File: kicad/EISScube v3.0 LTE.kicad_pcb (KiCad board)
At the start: 4 copper layers, 100 x 72 mm, 255 parts, among them J1 Boot, J2 UART, J3 JTag, J4 SIM_Card_w_det_sw, J5 USB_B_Mini, J6 Screw_Terminal_01x08, K1 SANYOU_SRD_Form_C, Q2 GSM3612PJZF, Q3 GSM3612PJZF, Q4 GSM3612PJZF, Q5 GSM3612PJZF, SW1 Reset, U1 STM32L051C8Tx, U2 SN74LV1T34DBVR, U3 U-Blox-SARA-R4, U4 LM2576HVS-12, U5 MIC29302WU-TR, U6 L7805, U7 LM1117-3.3, U8 LM1117-1.8, U9 LTV-357T, Y1 12MHz, Y2 32.768KHz

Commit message: Changes for enclosure case
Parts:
- removed the REF** at (160.0, 122.2)
- removed the REF** at (180.3, 122.6)
- removed the REF** at (180.3, 115.4)
- removed the REF** at (180.3, 110.4)
- removed the REF** at (180.3, 105.4)
- removed the REF** at (185.4, 122.6)
- removed the REF** at (175.3, 122.6)
- removed the REF** at (128.8, 94.3)
- removed the REF** at (138.8, 94.3)
- removed the REF** at (143.8, 89.3)
- removed the REF** at (120.4, 123.1)
- removed the REF** at (121.4, 124.2)
- removed the REF** at (114.6, 126.0)
- removed the REF** at (115.1, 121.0)
- added REF**: VIA-0.6mm, EISScube_LTE:VIA-0.6mm, F.Cu at (134.4, 126.0)
- added REF**: VIA-0.6mm, EISScube_LTE:VIA-0.6mm, F.Cu at (104.9, 116.3)
- added REF**: VIA-0.6mm, EISScube_LTE:VIA-0.6mm, F.Cu at (170.1, 111.3)
- added REF**: VIA-0.6mm, EISScube_LTE:VIA-0.6mm, F.Cu at (168.5, 112.8)
- added REF**: VIA-0.6mm, EISScube_LTE:VIA-0.6mm, F.Cu at (166.9, 114.4)
- added REF**: VIA-0.6mm, EISScube_LTE:VIA-0.6mm, F.Cu at (165.2, 116.1)
- added REF**: VIA-0.6mm, EISScube_LTE:VIA-0.6mm, F.Cu at (173.0, 124.5)
- added REF**: VIA-0.6mm, EISScube_LTE:VIA-0.6mm, F.Cu at (173.0, 123.2)
- added REF**: VIA-0.6mm, EISScube_LTE:VIA-0.6mm, F.Cu at (162.8, 121.9)
- added REF**: VIA-0.6mm, EISScube_LTE:VIA-0.6mm, F.Cu at (162.8, 124.5)
- added REF**: VIA-0.6mm, EISScube_LTE:VIA-0.6mm, F.Cu at (169.2, 118.4)
- added REF**: VIA-0.6mm, EISScube_LTE:VIA-0.6mm, F.Cu at (167.9, 124.5)
- added REF**: VIA-0.6mm, EISScube_LTE:VIA-0.6mm, F.Cu at (175.3, 115.7)
- added REF**: VIA-0.6mm, EISScube_LTE:VIA-0.6mm, F.Cu at (135.4, 123.7)
- added REF**: VIA-0.6mm, EISScube_LTE:VIA-0.6mm, F.Cu at (177.8, 115.7)
- added REF**: VIA-0.6mm, EISScube_LTE:VIA-0.6mm, F.Cu at (167.9, 121.9)
- added REF**: VIA-0.6mm, EISScube_LTE:VIA-0.6mm, F.Cu at (167.9, 119.8)
- added REF**: VIA-0.6mm, EISScube_LTE:VIA-0.6mm, F.Cu at (170.7, 116.8)
- added REF**: VIA-0.6mm, EISScube_LTE:VIA-0.6mm, F.Cu at (172.7, 115.7)
- added REF**: VIA-0.6mm, EISScube_LTE:VIA-0.6mm, F.Cu at (180.3, 115.7)
- added REF**: VIA-0.6mm, EISScube_LTE:VIA-0.6mm, F.Cu at (182.9, 115.7)
- added REF**: VIA-0.6mm, EISScube_LTE:VIA-0.6mm, F.Cu at (133.3, 123.7)
- added REF**: VIA-0.6mm, EISScube_LTE:VIA-0.6mm, F.Cu at (148.0, 118.7)
- added REF**: VIA-0.6mm, EISScube_LTE:VIA-0.6mm, F.Cu at (149.2, 114.9)
- added REF**: VIA-0.6mm, EISScube_LTE:VIA-0.6mm, F.Cu at (155.6, 112.4)
- added REF**: VIA-0.6mm, EISScube_LTE:VIA-0.6mm, F.Cu at (155.6, 114.9)
- added REF**: VIA-0.6mm, EISScube_LTE:VIA-0.6mm, F.Cu at (155.6, 121.3)
- added REF**: VIA-0.6mm, EISScube_LTE:VIA-0.6mm, F.Cu at (153.0, 121.3)
- AE1: value Antenna_Shield -> Antenna
- C35, C36, C37, C8, R24: moved to F.Cu
- J4: value SIM_Card_w_det_sw -> SIM card holder
- J6: value Screw_Terminal_01x08 -> Connector 1 x 8
- K1: value SANYOU_SRD_Form_C -> SRD Form C
- R23: moved to B.Cu
- REF**: footprint Mounting_Holes:MountingHole_3.2mm_M3_Pad_Via -> Mounting_Holes:MountingHole_2.7mm_Pad
- REF** (x3): footprint Mounting_Holes:MountingHole_3.2mm_M3_Pad_Via -> Mounting_Holes:MountingHole_2.7mm_M2.5_Pad
- moved REF** 67.9 mm to (103.5, 132.1)
- moved REF** 63.4 mm to (99.7, 132.1)
- moved REF** 50.1 mm to (99.7, 117.5)
- moved REF** 49.2 mm to (99.7, 81.3)
- moved REF** 48.3 mm to (99.7, 113.7)
- moved REF** 48.0 mm to (103.5, 109.9)
- moved REF** 44.0 mm to (99.7, 106.0)
- moved D10 38.6 mm to (137.7, 82.5), turned to 270 degrees
- moved REF** 36.3 mm to (112.4, 87.6)
- moved D8 35.8 mm to (135.1, 82.5), turned to 270 degrees
- moved D11 34.3 mm to (141.1, 98.3), turned to 90 degrees
- moved REF** 33.9 mm to (108.6, 87.0)
- moved C41 33.2 mm to (149.1, 121.2), turned to 180 degrees
- moved REF** 33.1 mm to (122.6, 110.5)
- moved C21 33.0 mm to (132.6, 82.4), turned to 90 degrees
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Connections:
- D14 pad 3: 24VAC-2 -> 24VAC-1
- D14 pad 4: 24VAC-1 -> 24VAC-2
- J4 pad C6: Net-(J4-PadC6) -> (no net)
- J5 pad 4: Net-(J5-Pad4) -> (no net)
- U1 pad 16: Net-(U1-Pad16) -> (no net)
- U1 pad 17: Net-(U1-Pad17) -> (no net)
- U1 pad 19: Net-(U1-Pad19) -> (no net)
- U1 pad 2: Net-(U1-Pad2) -> (no net)
- U1 pad 20: Net-(U1-Pad20) -> (no net)
- U1 pad 25: Net-(U1-Pad25) -> (no net)
- U1 pad 26: Net-(U1-Pad26) -> (no net)
- U1 pad 27: Net-(U1-Pad27) -> (no net)
- U1 pad 28: Net-(U1-Pad28) -> (no net)
- U1 pad 29: Net-(U1-Pad29) -> (no net)
- U1 pad 38: Net-(U1-Pad38) -> (no net)
- U1 pad 41: Net-(U1-Pad41) -> (no net)
- U1 pad 42: Net-(U1-Pad42) -> (no net)
- U1 pad 43: Net-(U1-Pad43) -> (no net)
- U1 pad 46: Net-(U1-Pad46) -> (no net)
- U2 pad 1: Net-(U2-Pad1) -> (no net)
- U3 pad 19: Net-(U3-Pad19) -> (no net)
- U3 pad 2: Net-(U3-Pad2) -> (no net)
- U3 pad 23: Net-(U3-Pad23) -> (no net)
- U3 pad 24: Net-(U3-Pad24) -> (no net)
- U3 pad 25: Net-(U3-Pad25) -> (no net)
- U3 pad 26: Net-(U3-Pad26) -> (no net)
- U3 pad 27: Net-(U3-Pad27) -> (no net)
- U3 pad 31: Net-(U3-Pad31) -> (no net)
- U3 pad 33: Net-(U3-Pad33) -> (no net)
- U3 pad 34: Net-(U3-Pad34) -> (no net)
- U3 pad 35: Net-(U3-Pad35) -> (no net)
- U3 pad 36: Net-(U3-Pad36) -> (no net)
- U3 pad 37: Net-(U3-Pad37) -> (no net)
- U3 pad 44: Net-(U3-Pad44) -> (no net)
- U3 pad 45: Net-(U3-Pad45) -> (no net)
- U3 pad 46: Net-(U3-Pad46) -> (no net)
- U3 pad 47: Net-(U3-Pad47) -> (no net)
- U3 pad 48: Net-(U3-Pad48) -> (no net)
- U3 pad 49: Net-(U3-Pad49) -> (no net)
- U3 pad 6: Net-(U3-Pad6) -> (no net)
- U3 pad 7: Net-(U3-Pad7) -> (no net)
- U3 pad 8: Net-(U3-Pad8) -> (no net)
- U3 pad 9: Net-(U3-Pad9) -> (no net)
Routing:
- net /EISScube-pw/COM: track 0.00 -> 133.3 mm
- net /EISScube-pw/NC: track 0.07 -> 108.1 mm
- net +12V: track 93.1 -> 131.3 mm, vias 2 -> 1
- net /EISScube-pw/NO: track 0.00 -> 27.4 mm
- net GND: track 55.8 -> 30.8 mm, vias 1 -> 0
- net /EISScube-cl/V_INT: track 50.3 -> 27.0 mm
- net +1V8: track 100.9 -> 120.4 mm
- net /EISScube-pw/+5V: track 39.4 -> 58.5 mm, vias 0 -> 1
- net +3V3: track 48.0 -> 64.5 mm, vias 1 -> 2
- net /EISScube-cl/VSIM: track 33.6 -> 48.4 mm
- net INPUT: track 56.9 -> 43.1 mm, vias 0 -> 1
- net /EISScube-cl/SIM_RST: track 33.7 -> 47.3 mm
- net NRST: track 43.1 -> 30.0 mm, vias 2 -> 1
- net Net-(D15-Pad1): track 18.5 -> 30.8 mm
- net /EISScube-cl/SIM_CLK: track 35.0 -> 46.4 mm
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- removed copper zone on B.Cu, net +12V
- removed copper zone on F.Cu, net +12V
- removed copper zone on In1.Cu, net +12V
- removed copper zone on In2.Cu, net +12V
- removed copper zone on B.Cu, net /EISScube-pw/COM
- removed copper zone on F.Cu, net /EISScube-pw/COM
- removed copper zone on In1.Cu, net /EISScube-pw/COM
- removed copper zone on In2.Cu, net /EISScube-pw/COM
- removed copper zone on B.Cu, net /EISScube-pw/NC
- removed copper zone on F.Cu, net /EISScube-pw/NC
- removed copper zone on In1.Cu, net /EISScube-pw/NC
- removed copper zone on In2.Cu, net /EISScube-pw/NC
- removed copper zone on B.Cu, net /EISScube-pw/NO
- removed copper zone on F.Cu, net /EISScube-pw/NO
- removed copper zone on In1.Cu, net /EISScube-pw/NO
- removed copper zone on In2.Cu, net /EISScube-pw/NO
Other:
- board size 100 x 72 mm -> 94 x 54 mm
- board text added: "EISScube LTE v.3.0"
- board text removed: "EISS Cube LTE"

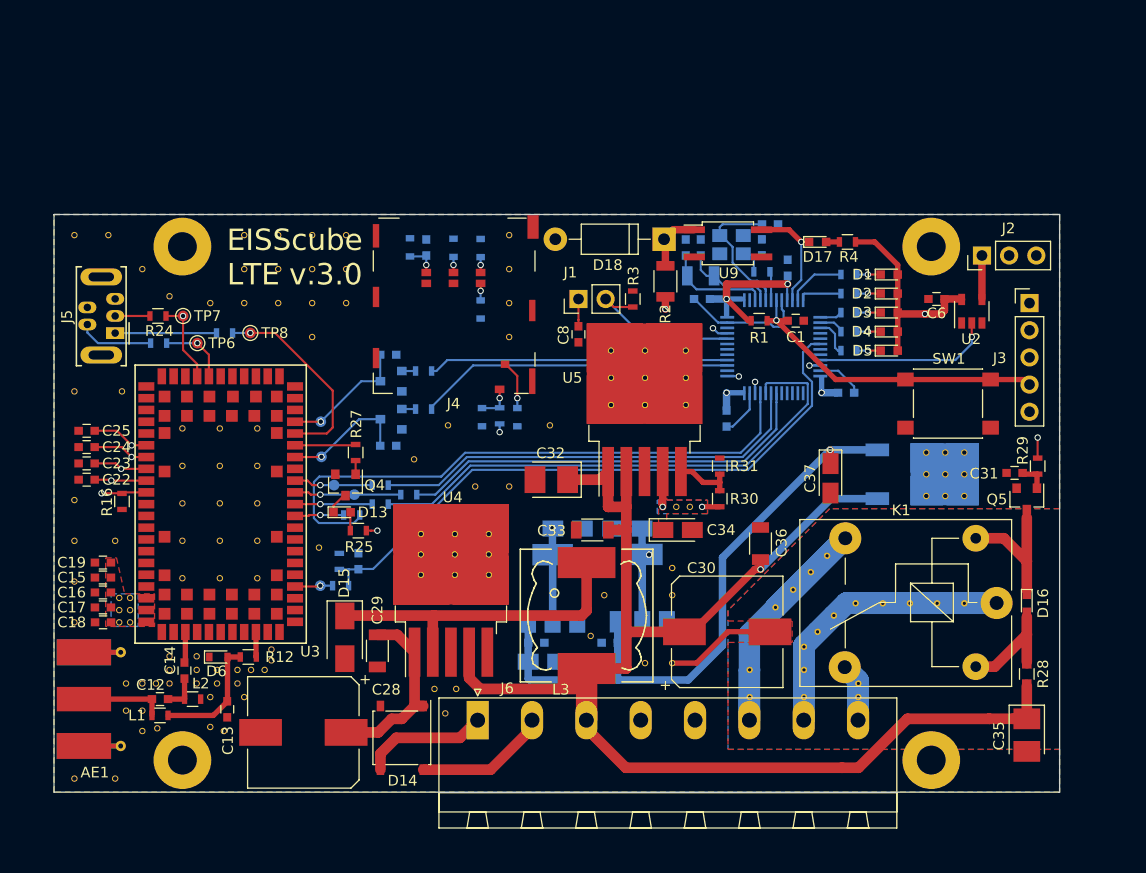
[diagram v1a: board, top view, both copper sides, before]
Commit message: add visual references are called “fiducials“ on board for PnP machine
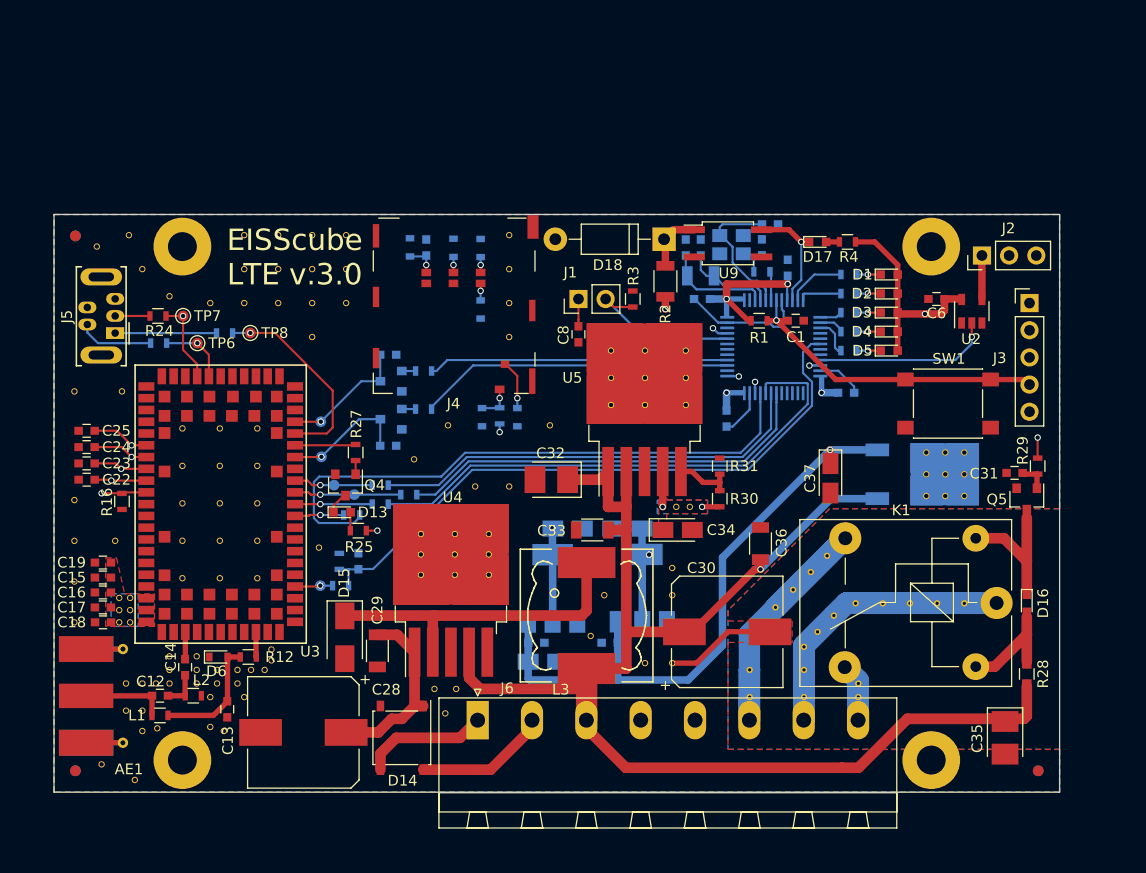
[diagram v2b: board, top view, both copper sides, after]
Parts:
- added FID1: Fiducial, Fiducials:Fiducial_1mm_Dia_2.54mm_Outer_CopperTop, F.Cu at (99.8, 131.3)
- added FID2: Fiducial, Fiducials:Fiducial_1mm_Dia_2.54mm_Outer_CopperTop, F.Cu at (189.8, 131.3)
- added FID3: Fiducial, Fiducials:Fiducial_1mm_Dia_2.54mm_Outer_CopperTop, F.Cu at (99.8, 81.3)
- added FID4: Fiducial, Fiducials:Fiducial_1mm_Dia_2.54mm_Outer_CopperBottom, F.Cu at (99.8, 131.3)
- added FID5: Fiducial, Fiducials:Fiducial_1mm_Dia_2.54mm_Outer_CopperBottom, F.Cu at (189.8, 131.3)
- added FID6: Fiducial, Fiducials:Fiducial_1mm_Dia_2.54mm_Outer_CopperBottom, F.Cu at (99.8, 81.3)
- AE1: value Antenna -> Antenna_Shield
- J4: value SIM card holder -> SIM_Card_w_det_sw
- J6: value Connector 1 x 8 -> Screw_Terminal_01x08
- K1: value SRD Form C -> SANYOU_SRD_Form_C
- moved REF** 2.87 mm to (102.2, 130.7)
- moved REF** 2.35 mm to (101.8, 82.3)
- moved C35 2.05 mm to (186.7, 128.3)
- moved REF** 1.92 mm to (104.8, 81.3)
- moved REF** 1.85 mm to (105.3, 132.2)
- moved AE1 0.37 mm to (102.5, 124.3)
- moved C14 0.32 mm to (110.0, 121.7)
- moved L2 0.32 mm to (110.8, 124.3)
- moved C12 0.32 mm to (107.7, 124.3)
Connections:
- J4 pad C6: (no net) -> Net-(J4-PadC6)
- J5 pad 4: (no net) -> Net-(J5-Pad4)
- U1 pad 16: (no net) -> Net-(U1-Pad16)
- U1 pad 17: (no net) -> Net-(U1-Pad17)
- U1 pad 19: (no net) -> Net-(U1-Pad19)
- U1 pad 2: (no net) -> Net-(U1-Pad2)
- U1 pad 20: (no net) -> Net-(U1-Pad20)
- U1 pad 25: (no net) -> Net-(U1-Pad25)
- U1 pad 26: (no net) -> Net-(U1-Pad26)
- U1 pad 27: (no net) -> Net-(U1-Pad27)
- U1 pad 28: (no net) -> Net-(U1-Pad28)
- U1 pad 29: (no net) -> Net-(U1-Pad29)
- U1 pad 38: (no net) -> Net-(U1-Pad38)
- U1 pad 41: (no net) -> Net-(U1-Pad41)
- U1 pad 42: (no net) -> Net-(U1-Pad42)
- U1 pad 43: (no net) -> Net-(U1-Pad43)
- U1 pad 46: (no net) -> Net-(U1-Pad46)
- U2 pad 1: (no net) -> Net-(U2-Pad1)
- U3 pad 19: (no net) -> Net-(U3-Pad19)
- U3 pad 2: (no net) -> Net-(U3-Pad2)
- U3 pad 23: (no net) -> Net-(U3-Pad23)
- U3 pad 24: (no net) -> Net-(U3-Pad24)
- U3 pad 25: (no net) -> Net-(U3-Pad25)
- U3 pad 26: (no net) -> Net-(U3-Pad26)
- U3 pad 27: (no net) -> Net-(U3-Pad27)
- U3 pad 31: (no net) -> Net-(U3-Pad31)
- U3 pad 33: (no net) -> Net-(U3-Pad33)
- U3 pad 34: (no net) -> Net-(U3-Pad34)
- U3 pad 35: (no net) -> Net-(U3-Pad35)
- U3 pad 36: (no net) -> Net-(U3-Pad36)
- U3 pad 37: (no net) -> Net-(U3-Pad37)
- U3 pad 44: (no net) -> Net-(U3-Pad44)
- U3 pad 45: (no net) -> Net-(U3-Pad45)
- U3 pad 46: (no net) -> Net-(U3-Pad46)
- U3 pad 47: (no net) -> Net-(U3-Pad47)
- U3 pad 48: (no net) -> Net-(U3-Pad48)
- U3 pad 49: (no net) -> Net-(U3-Pad49)
- U3 pad 6: (no net) -> Net-(U3-Pad6)
- U3 pad 7: (no net) -> Net-(U3-Pad7)
- U3 pad 8: (no net) -> Net-(U3-Pad8)
- U3 pad 9: (no net) -> Net-(U3-Pad9)

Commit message: changes for new case RL6015
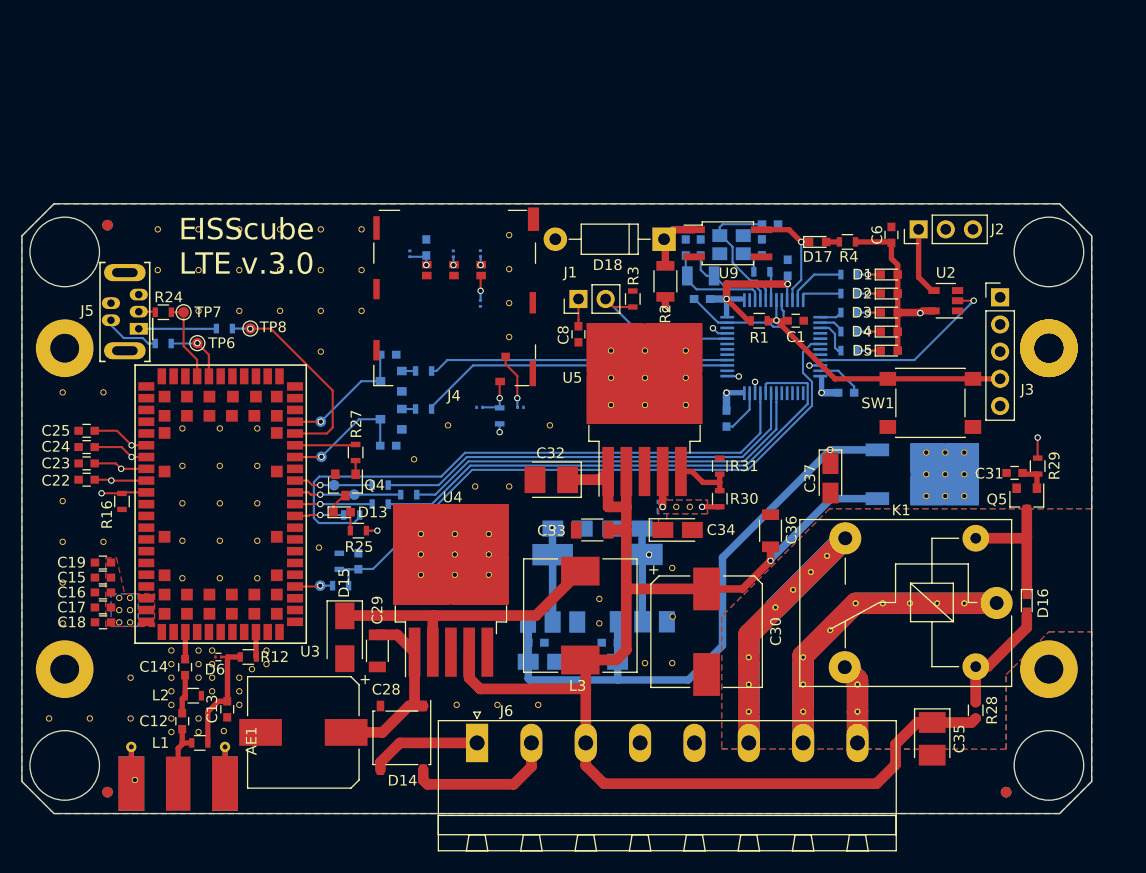
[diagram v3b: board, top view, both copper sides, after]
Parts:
- removed the REF** at (169.2, 118.4)
- added REF**: VIA-0.6mm, EISScube_LTE:VIA-0.6mm, F.Cu at (162.7, 120.7)
- added REF**: MountingHole_6mm, Mounting_Holes:MountingHole_6.5mm, F.Cu at (190.8, 82.8)
- added REF**: MountingHole_6mm, Mounting_Holes:MountingHole_6.5mm, F.Cu at (190.8, 130.8)
- added REF**: MountingHole_6mm, Mounting_Holes:MountingHole_6.5mm, F.Cu at (98.8, 130.8)
- added REF**: MountingHole_6mm, Mounting_Holes:MountingHole_6.5mm, F.Cu at (98.8, 82.8)
- added REF**: VIA-0.6mm, EISScube_LTE:VIA-0.6mm, F.Cu at (105.0, 122.7)
- added REF**: MountingHole_3.2mm_M3_Pad_Via, Mounting_Holes:MountingHole_2.7mm_M2.5_Pad, F.Cu at (190.8, 91.8)
- AE1: value Antenna_Shield -> Antenna
- D10, D11, D12, D6, D7, D8, D9: footprint Diodes_SMD:D_0603 -> Inductors_SMD:L_0201
- FID1, FID2, FID3: footprint Fiducials:Fiducial_1mm_Dia_2.54mm_Outer_CopperTop -> Fiducials:Fiducial_1mm_Dia_2mm_Outer
- FID4, FID5, FID6: footprint Fiducials:Fiducial_1mm_Dia_2.54mm_Outer_CopperBottom -> Fiducials:Fiducial_1mm_Dia_2mm_Outer; moved to B.Cu
- L3: footprint Choke_SMD:Choke_SMD_12x12mm_h8mm -> Inductors_SMD:L_10.4x10.4_H4.8
- moved REF** 14.5 mm to (190.8, 91.8)
- moved REF** 14.5 mm to (98.8, 91.8)
- moved REF** 13.9 mm to (98.8, 121.8)
- moved REF** 13.9 mm to (190.8, 121.8)
- moved AE1 9.46 mm to (109.4, 130.8), turned to 90 degrees
- moved REF** 8.72 mm to (143.1, 125.2)
- moved C6 7.32 mm to (176.1, 81.3), turned to 90 degrees
- moved C35 6.81 mm to (179.9, 128.4)
- moved REF** 6.53 mm to (111.3, 80.7)
- moved REF** 6.51 mm to (97.3, 126.5)
- moved J2 6.41 mm to (178.6, 80.7)
- moved REF** 5.92 mm to (107.5, 80.7)
- moved R28 5.86 mm to (183.9, 125.7)
- moved REF** 5.26 mm to (111.3, 127.7)
- moved REF** 5.26 mm to (111.3, 84.5)
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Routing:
- net /EISScube-pw/NC: track 108.1 -> 122.0 mm
- net GND: track 30.8 -> 20.5 mm
- net +12V: track 131.3 -> 125.2 mm
- net Net-(D15-Pad1): track 30.8 -> 27.3 mm
- net /EISScube-mc/RX_H: track 27.5 -> 24.0 mm
- net +3V3: track 64.5 -> 61.0 mm
- net +1V8: track 120.4 -> 117.5 mm
- net NRST: track 30.0 -> 27.0 mm
- net /EISScube-pw/NO: track 27.4 -> 30.3 mm
- net /EISScube-mc/SWCLK: track 31.9 -> 29.3 mm
- net /EISScube-mc/SWDIO: track 28.7 -> 26.2 mm
- net /EISScube-mc/TX_H: track 4.13 -> 6.44 mm
- net Net-(J5-Pad1): track 9.48 -> 7.26 mm
- net INPUT: track 43.1 -> 45.2 mm
- net Net-(AE1-Pad1): track 8.00 -> 6.14 mm
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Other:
- board size 94 x 54 mm -> 100 x 57 mm

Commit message: sent to Chin-Tec
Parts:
- moved REF** 2.16 mm to (155.5, 119.1)
- moved J1 0.60 mm to (146.8, 87.9)
- moved R3 0.16 mm to (151.9, 87.1)
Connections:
- J4 pad 10: (no net) -> GND
- J4 pad 11: (no net) -> GND
- J4 pad 7: (no net) -> GND
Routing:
- net NRST: track 27.0 -> 29.0 mm
- net /EISScube-cl/VSIM: track 47.7 -> 49.1 mm
- net /EISScube-cl/SIM_DTK: track 52.0 -> 52.6 mm
- net /EISScube-mc/BOOT0: track 15.8 -> 15.2 mm

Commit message: moved LEDs on bottom side. Created a custome bottom part of enclosure RL6015
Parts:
- removed the REF** at (155.6, 112.4)
- AE1: value Antenna -> Antenna_Shield
- C28: value 470uF 35V -> 220uF 35V
- C30: value 330uF 16V -> 680uF 16V
- C31, C35, C6, D1, D16, D17, D2, D3, D4, D5, Q5, R28, R29, R4: moved to B.Cu
- moved R28 29.6 mm to (173.5, 98.0), turned to 180 degrees
- moved D16 24.6 mm to (175.1, 95.2), turned to 180 degrees
- moved D17 5.99 mm to (175.1, 83.0)
- moved C37 5.60 mm to (164.8, 104.0)
- moved Q5 5.04 mm to (185.0, 102.6), turned to 180 degrees
- moved REF** 4.64 mm to (176.5, 102.9)
- moved REF** 4.64 mm to (176.5, 100.8)
- moved REF** 4.64 mm to (176.5, 104.9)
- moved REF** 4.64 mm to (174.8, 100.8)
- moved REF** 4.64 mm to (174.8, 102.9)
- moved REF** 4.64 mm to (174.8, 104.9)
- moved REF** 4.64 mm to (178.3, 100.8)
- moved REF** 4.64 mm to (178.3, 102.9)
- moved REF** 4.64 mm to (178.3, 104.9)
- moved U6 4.44 mm to (174.6, 102.8)
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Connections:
- D17 pad 2: Net-(D17-Pad2) -> +3V3
- J4 pad 10: GND -> (no net)
- J4 pad 11: GND -> (no net)
- J4 pad 7: GND -> (no net)
- K1 pad 5: Net-(D16-Pad2) -> +12V
- R4 pad 1: Net-(D17-Pad2) -> Net-(R4-Pad1)
- R4 pad 2: +3V3 -> Net-(D17-Pad1)
- U1 pad 10: Net-(D17-Pad1) -> Net-(R4-Pad1)
- U9 pad 4: Net-(D17-Pad1) -> Net-(R4-Pad1)
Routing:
- net Net-(R4-Pad1): track 0.00 -> 13.9 mm, vias 0 -> 1
- net Net-(D17-Pad1): track 10.7 -> 1.24 mm, vias 1 -> 0
- net +12V: track 125.2 -> 133.7 mm
- net Net-(D16-Pad2): track 11.2 -> 2.80 mm
- net Net-(D16-Pad1): track 12.8 -> 19.1 mm
- net +1V8: track 117.4 -> 123.6 mm
- net RELAY: track 41.8 -> 39.1 mm
- net +3V3: track 61.5 -> 59.5 mm
- net /EISScube-pw/+5V: track 58.5 -> 57.1 mm
- net Net-(D17-Pad2): track 1.24 -> 0.00 mm
- net Net-(C31-Pad1): track 2.80 -> 3.88 mm
- net Net-(D5-Pad1): track 2.21 -> 1.24 mm, vias 1 -> 0
- net Net-(D4-Pad1): track 2.21 -> 1.24 mm, vias 1 -> 0
- net Net-(D3-Pad1): track 2.21 -> 1.24 mm, vias 1 -> 0
- net Net-(D2-Pad1): track 2.21 -> 1.24 mm, vias 1 -> 0
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
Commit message: migration to new version of KiCAD v.6.x
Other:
- net class Default removed
